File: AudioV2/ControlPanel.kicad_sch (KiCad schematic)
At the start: 39 parts, among them SW1 PWR SW, SW2 DEST sense (3PDT 3rd pole), U1 Pico 2 / RP2350, U2 PT2314-D, U5 BP5293-50 +5V

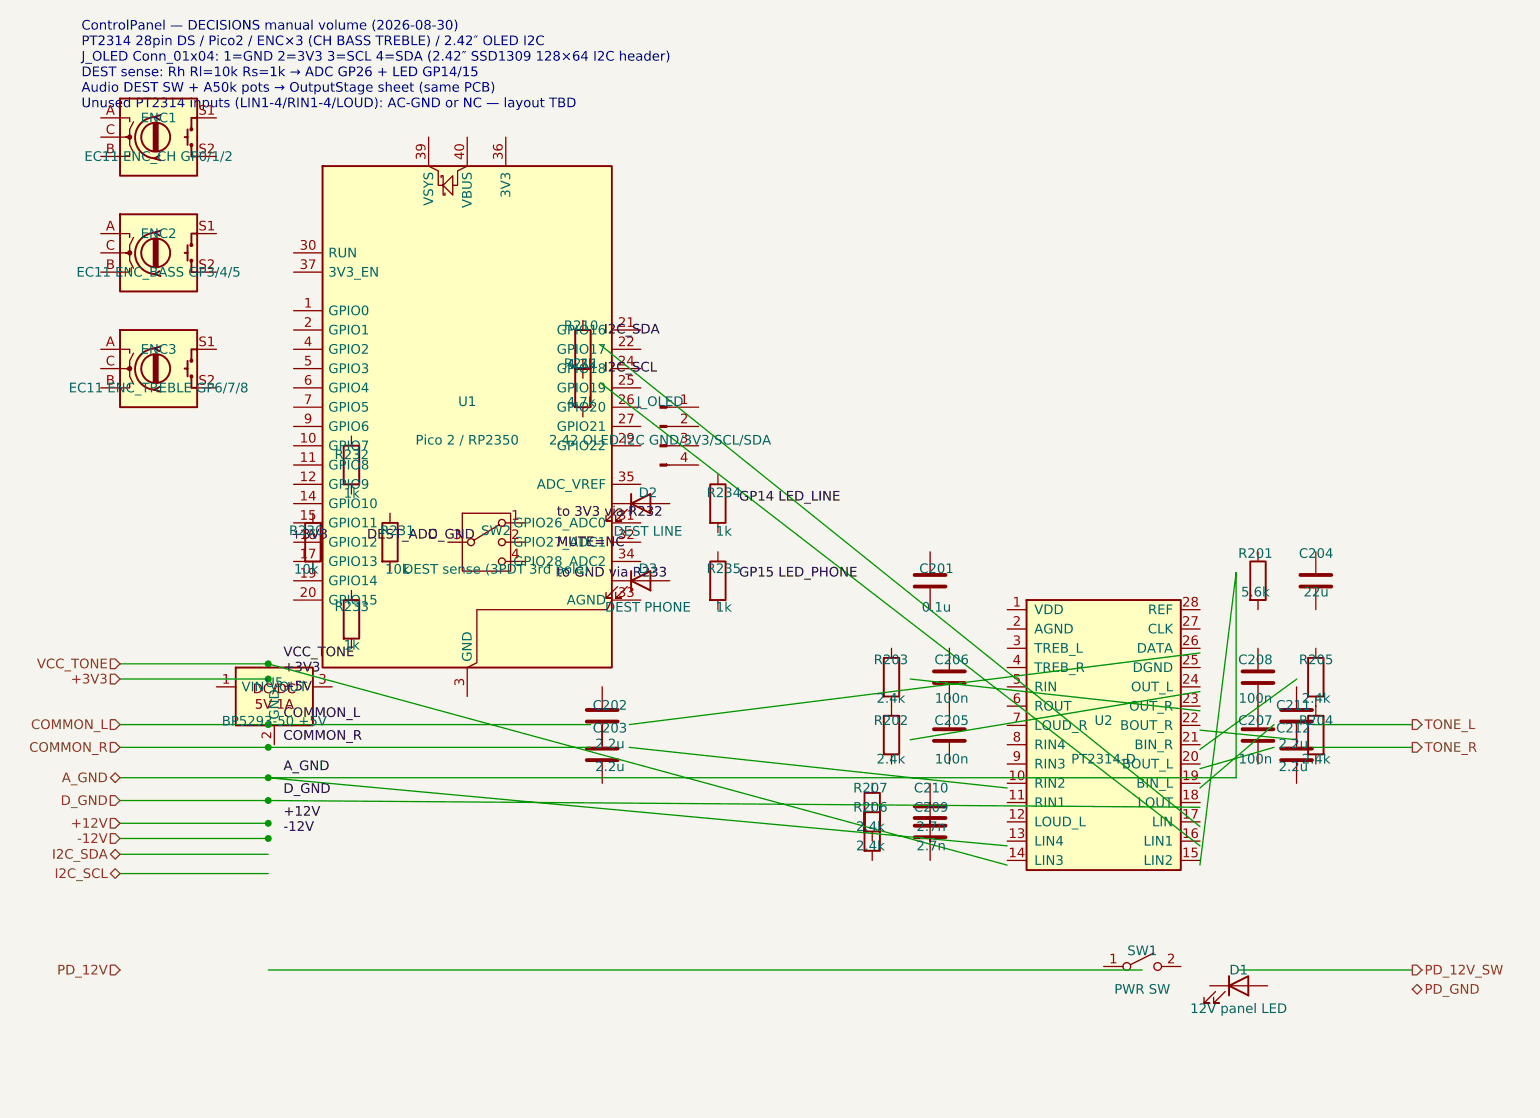
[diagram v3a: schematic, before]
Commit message: AudioV2: ラベル結線で Power/Control/Output をネット接続
pin_connect を tip=(at) 基準に修正し、同名ローカルラベルをピン tip に
載せて結線。グリッドスナップ一致・パッシブ間隔・親シートピン橋渡しを
整え、一次 PD_GND と二次 A_GND の分離を維持。
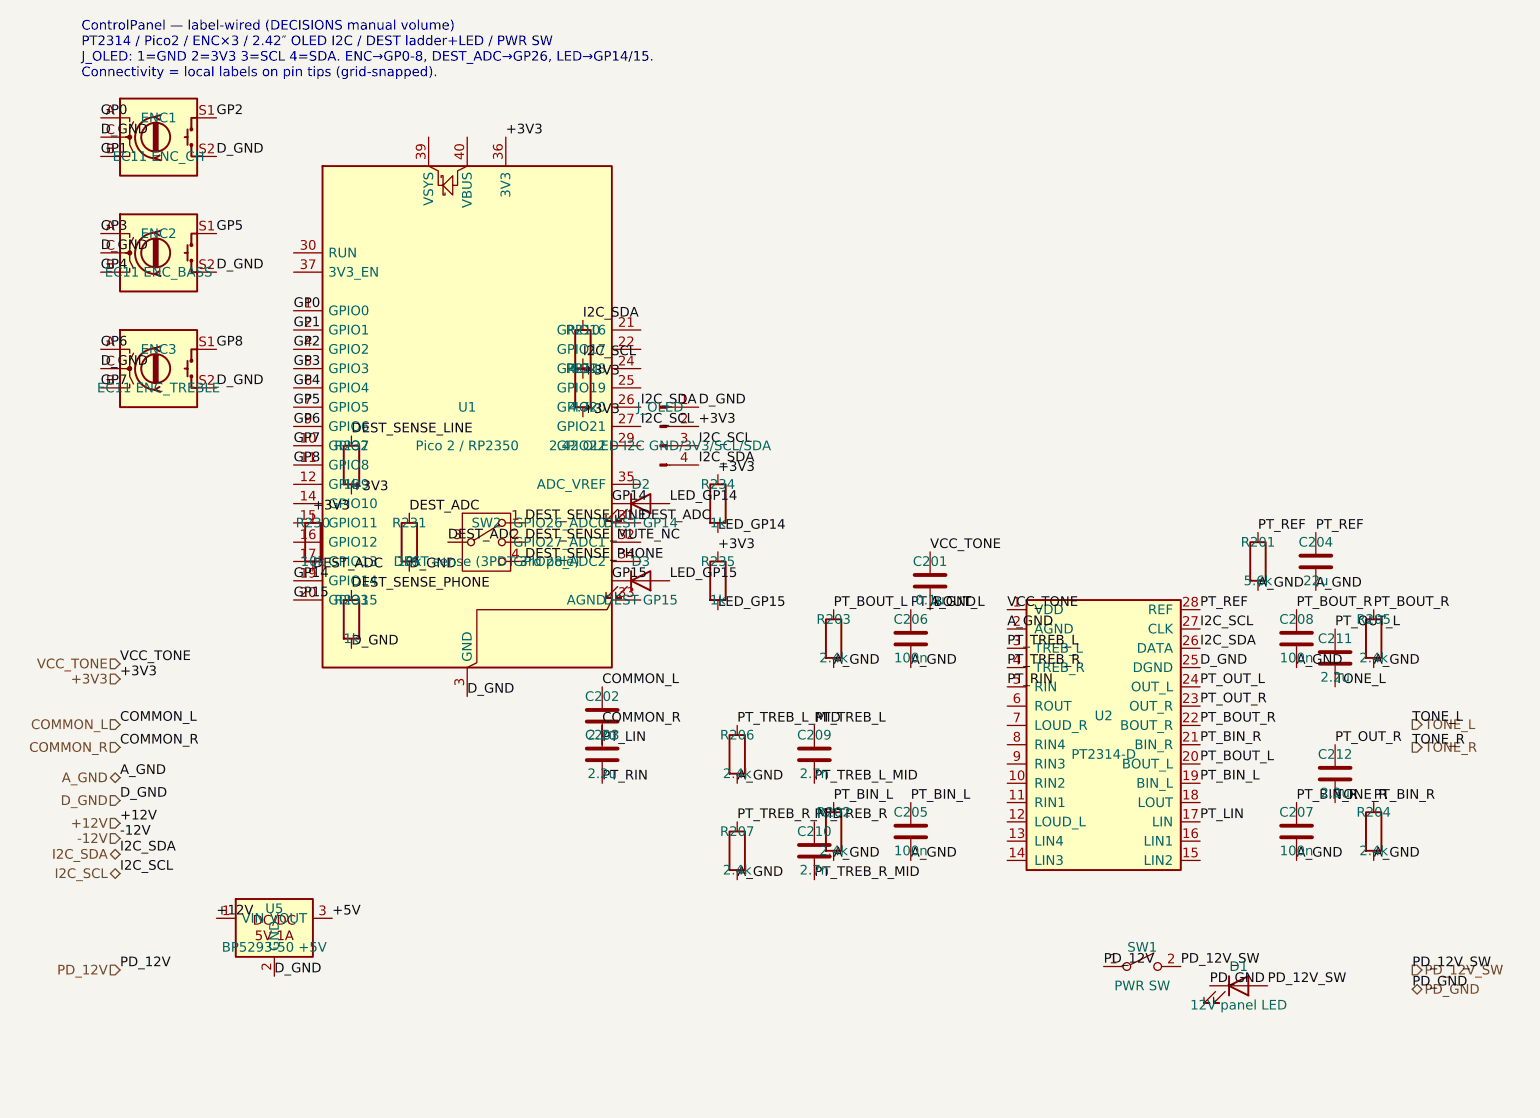
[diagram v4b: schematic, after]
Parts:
- D2: value DEST LINE -> DEST GP14
- D3: value DEST PHONE -> DEST GP15
- ENC1: value EC11 ENC_CH GP0/1/2 -> EC11 ENC_CH
- ENC2: value EC11 ENC_BASS GP3/4/5 -> EC11 ENC_BASS
- ENC3: value EC11 ENC_TREBLE GP6/7/8 -> EC11 ENC_TREBLE
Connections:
- net +12V: now also U5.1 (VIN)
- net +3V3: now also J_OLED.2 (Pin_2), R210.2, R211.2, R230.1, R232.2, R234.1, R235.1, U1.36 (3V3)
- net +5V: now also U5.3 (VOUT)
- net A_GND: now also C201.2, C204.2, C205.2, C206.2, C207.2, C208.2, R201.2, R202.2, R203.2, R204.2, R205.2, R206.2, R207.2, U2.2 (AGND)
- net COMMON_L: now also C202.1
- net COMMON_R: now also C203.1
- net DEST_ADC: now also R230.2, R231.1, SW2.3, U1.31 (GPIO26_ADC0)
- net D_GND: now also ENC1.C, ENC1.S2, ENC2.C, ENC2.S2, ENC3.C, ENC3.S2, J_OLED.1 (Pin_1), R231.2, R233.2, U1.13 (GND), U1.18 (GND), U1.23 (GND), U1.28 (GND), U1.3 (GND), U1.38 (GND), U1.8 (GND), U2.25 (DGND), U5.2 (GND)
- net I2C_SCL: now also J_OLED.3 (Pin_3), R211.1, U1.27 (GPIO21), U2.27 (CLK)
- net I2C_SDA: now also J_OLED.4 (Pin_4), R210.1, U1.26 (GPIO20), U2.26 (DATA)
- net PD_12V: now also SW1.1 (A)
- net PD_12V_SW: now also D1.2 (A), SW1.2 (B)
- net PD_GND: now also D1.1 (K)
- net TONE_L: now also C211.2
- net TONE_R: now also C212.2
- net VCC_TONE: now also C201.1, U2.1 (VDD)
- net PT_RIN: now reaches C203.2
- net PT_RIN: now also U2.5 (RIN)
- net PT_BIN_L: now reaches R202.1
- net PT_BIN_L: now also C205.1, U2.19 (BIN_L); no longer R203.2
- net PT_LIN: now reaches C202.2
- net PT_LIN: now also U2.17 (LIN)
- net PT_BIN_R: now reaches C207.1
- net PT_BIN_R: now also R204.1, U2.21 (BIN_R); no longer C208.2
- net LED_GP15: now reaches R235.2
- net LED_GP15: now also D3.2 (A)
- net PT_REF: now reaches C204.1
- net PT_REF: now also R201.1, U2.28 (REF)
- net GP6: now reaches ENC3.A
- net GP6: now also U1.9 (GPIO6)
- net GP7: now reaches ENC3.B
- net GP7: now also U1.10 (GPIO7)
- net GP8: now reaches ENC3.S1
- net GP8: now also U1.11 (GPIO8)
- net PT_BOUT_L: now reaches C206.1
- net PT_BOUT_L: now also R203.1, U2.20 (BOUT_L)
- net GP0: now reaches U1.1 (GPIO0)
- net GP0: now also ENC1.A
- net GP14: now reaches U1.19 (GPIO14)
- net GP14: now also D2.1 (K)
- net GP1: now reaches U1.2 (GPIO1)
- net GP1: now also ENC1.B
- net GP15: now reaches U1.20 (GPIO15)
- net GP15: now also D3.1 (K)
- net GP2: now reaches U1.4 (GPIO2)
- net GP2: now also ENC1.S1
- net GP3: now reaches U1.5 (GPIO3)
- net GP3: now also ENC2.A
- net GP4: now reaches U1.6 (GPIO4)
- net GP4: now also ENC2.B
- net GP5: now reaches U1.7 (GPIO5)
- net GP5: now also ENC2.S1
- net PT_TREB_L: now reaches C209.1
- net PT_TREB_L: now also U2.3 (TREB_L)
- net PT_TREB_L_MID: now reaches C209.2
- net PT_TREB_L_MID: now also R206.1
- net PT_TREB_R_MID: now reaches R207.1
- net PT_TREB_R_MID: now also C210.2
- net PT_BOUT_R: now reaches U2.22 (BOUT_R)
- net PT_BOUT_R: now also C208.1, R205.1
- net PT_OUT_R: now reaches U2.23 (OUT_R)
- net PT_OUT_R: now also C212.1
- net PT_OUT_L: now reaches U2.24 (OUT_L)
- net PT_OUT_L: now also C211.1
- net PT_TREB_R: now reaches U2.4 (TREB_R)
- net PT_TREB_R: now also C210.1
- net DEST_SENSE_PHONE: now reaches R233.1
- net DEST_SENSE_PHONE: now also SW2.4
- net DEST_SENSE_LINE: now reaches SW2.1
- net DEST_SENSE_LINE: now also R232.1
- net DEST_SENSE_MUTE_NC: now reaches SW2.2
- net LED_GP14: now reaches D2.2 (A)
- net LED_GP14: now also R234.2
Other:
- note added: "ControlPanel — label-wired (DECISIONS manual volume) PT2314 / Pico2 / ENC×3 / 2.42″ OLED I2C / DEST ladder+LED / PWR SW J_OLED: 1=GND 2=3V3 3=SCL 4=SDA. ENC→GP0-8, DEST_ADC→GP26, LED→GP14/15. Connectivity = local labels on pin tips (grid-snapped)."
- note removed: "ControlPanel — DECISIONS manual volume (2026-08-30) PT2314 28pin DS / Pico2 / ENC×3 (CH BASS TREBLE) / 2.42″ OLED I2C J_OLED Conn_01x04: 1=GND 2=3V3 3=SCL 4=SDA (2.42″ SSD1309 128×64 I2C header) DEST sense: Rh Rl=10k Rs=1k → ADC GP26 + LED GP14/15 Audio DEST SW + A50k pots → OutputStage sheet (same PCB) Unused PT2314 inputs (LIN1-4/RIN1-4/LOUD): AC-GND or NC — layout TBD"
